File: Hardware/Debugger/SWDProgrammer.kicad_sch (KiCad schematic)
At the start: 37 parts, among them J1 USB_C_Receptacle_USB2.0, J2 USB_C_Receptacle_USB2.0, U1 AP2112K-3.3, U2 STM32F103C8Tx, Y1 32.768KHZ, Y2 8Mhz

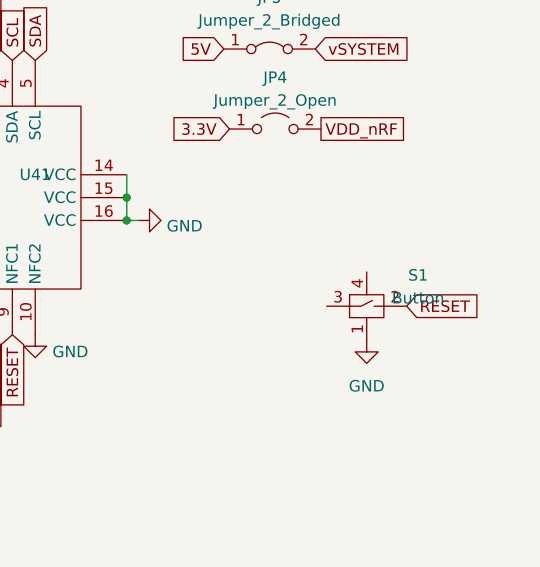
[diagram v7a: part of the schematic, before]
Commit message: migrated components to 0201
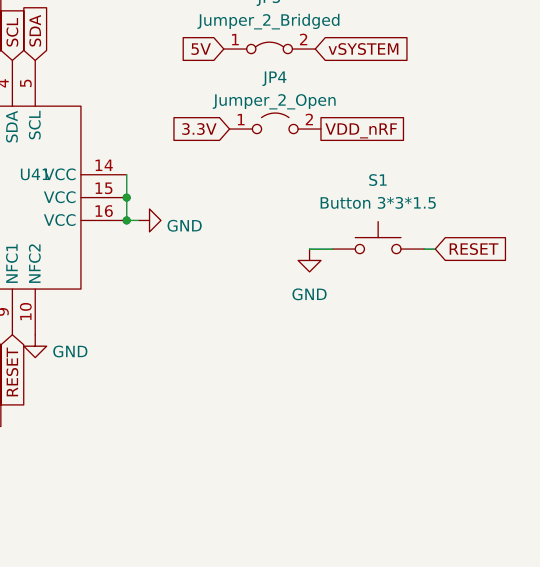
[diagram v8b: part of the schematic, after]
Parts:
- removed S1: Button, Library:button 3x3, symbol Library:Button
- added S1: Button 3*3*1.5, Library:button 3x3, symbol Switch:SW_Push
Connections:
- net GND: now also S1.1
- net RESET: now also S1.2
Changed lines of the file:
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@@
 	(wire
 		(pts
+			(xy 247.65 130.81) (xy 250.19 130.81)
+		)
+		(stroke
+			(width 0)
+			(type default)
+		)
+	)
+	(wire
+		(pts
 			(xy 131.445 20.955) (xy 140.335 20.955)
 		)
@@
 	(wire
 		(pts
+			(xy 261.62 130.81) (xy 260.35 130.81)
+		)
+		(stroke
+			(width 0)
+			(type default)
+		)
+	)
+	(wire
+		(pts
 			(xy 114.935 72.39) (xy 108.585 72.39)
 		)
@@
 		)
 	)
-	(global_label "RESET"
-		(shape input)
-		(at 258.445 137.16 0)
-		(fields_autoplaced yes)
-		(effects
-			(font
-				(size 1.27 1.27)
-			)
-			(justify left)
-		)
-		(property "Intersheetrefs" "${INTERSHEET_REFS}"
-			(at 267.0959 137.16 0)
-			(effects
-				(font
-					(size 1.27 1.27)
-				)
-				(justify left)
-				(hide yes)
-			)
-		)
-	)
 	(global_label "3.3V"
 		(shape input)
@@
 		)
 	)
+	(global_label "RESET"
+		(shape input)
+		(at 261.62 130.81 0)
+		(fields_autoplaced yes)
+		(effects
+			(font
+				(size 1.27 1.27)
+			)
+			(justify left)
+		)
+		(property "Intersheetrefs" "${INTERSHEET_REFS}"
+			(at 270.2709 130.81 0)
+			(effects
+				(font
+					(size 1.27 1.27)
+				)
+				(justify left)
+				(hide yes)
+			)
+		)
+	)
 	(global_label "3.3V"
 		(shape input)
@@
 	)
 	(symbol
-		(lib_id "power:GND")
-		(at 254 140.97 0)
-		(unit 1)
-		(exclude_from_sim no)
-		(in_bom yes)
-		(on_board yes)
-		(dnp no)
-		(fields_autoplaced yes)
-		(property "Reference" "#PWR026"
-			(at 254 147.32 0)
-			(effects
-				(font
-					(size 1.27 1.27)
-				)
-				(hide yes)
-			)
-		)
-		(property "Value" "GND"
-			(at 254 146.05 0)
-			(effects
-				(font
-					(size 1.27 1.27)
-				)
-			)
-		)
-		(property "Footprint" ""
-			(at 254 140.97 0)
-			(effects
-				(font
-					(size 1.27 1.27)
-				)
-				(hide yes)
-			)
-		)
-		(property "Datasheet" ""
-			(at 254 140.97 0)
-			(effects
-				(font
-					(size 1.27 1.27)
-				)
-				(hide yes)
-			)
-		)
-		(property "Description" ""
-			(at 254 140.97 0)
-			(effects
-				(font
-					(size 1.27 1.27)
-				)
-				(hide yes)
-			)
-		)
-		(pin "1"
-		)
-		(instances
-			(project "SWDProgrammer"
-				(path "/c10d4a68-1c04-4145-8c29-cc9b9e805c41"
-					(reference "#PWR026")
-					(unit 1)
-				)
-			)
-			(project "Revolute"
-				(path "/e63e39d7-6ac0-4ffd-8aa3-1841a4541b55"
-					(reference "#PWR034")
-					(unit 1)
-				)
-			)
-			(project "TopPCB"
-				(path "/ea7d4d47-b765-4ea1-81d3-52cfadd68d8d"
-					(reference "#PWR01")
-					(unit 1)
-				)
-			)
-		)
-	)
-	(symbol
 		(lib_id "Device:C")
 		(at 26.67 74.93 270)
@@
 	)
 	(symbol
+		(lib_id "Switch:SW_Push")
+		(at 255.27 130.81 0)
+		(unit 1)
+		(exclude_from_sim no)
+		(in_bom yes)
+		(on_board yes)
+		(dnp no)
+		(fields_autoplaced yes)
+		(property "Reference" "S1"
+			(at 255.27 123.19 0)
+			(effects
+				(font
+					(size 1.27 1.27)
+				)
+			)
+		)
+		(property "Value" "Button 3*3*1.5"
+			(at 255.27 125.73 0)
+			(effects
+				(font
+					(size 1.27 1.27)
+				)
+			)
+		)
+		(property "Footprint" "Library:button 3x3"
+			(at 255.27 125.73 0)
+			(effects
+				(font
+					(size 1.27 1.27)
+				)
+				(hide yes)
+			)
+		)
+		(property "Datasheet" "~"
+			(at 255.27 125.73 0)
+			(effects
+				(font
+					(size 1.27 1.27)
+				)
+				(hide yes)
+			)
+		)
+		(property "Description" "Push button switch, generic, two pins"
+			(at 255.27 130.81 0)
+			(effects
+				(font
+					(size 1.27 1.27)
+				)
+				(hide yes)
+			)
+		)
+		(property "ID" "111"
+			(at 255.27 130.81 0)
+			(effects
+				(font
+					(size 1.27 1.27)
+				)
+				(hide yes)
+			)
+		)
+		(pin "2"
+		)
+		(pin "1"
+		)
+		(instances
+			(project "SWDProgrammer"
+				(path "/c10d4a68-1c04-4145-8c29-cc9b9e805c41"
+					(reference "S1")
+					(unit 1)
+				)
+			)
+		)
+	)
+	(symbol
 		(lib_id "power:GND")
 		(at 180.975 53.975 0)
@@
 	(symbol
 		(lib_id "power:GND")
+		(at 247.65 130.81 0)
+		(unit 1)
+		(exclude_from_sim no)
+		(in_bom yes)
+		(on_board yes)
+		(dnp no)
+		(fields_autoplaced yes)
+		(property "Reference" "#PWR027"
+			(at 247.65 137.16 0)
+			(effects
+				(font
+					(size 1.27 1.27)
+				)
+				(hide yes)
+			)
+		)
+		(property "Value" "GND"
+			(at 247.65 135.89 0)
+			(effects
+				(font
+					(size 1.27 1.27)
+				)
+			)
+		)
+		(property "Footprint" ""
+			(at 247.65 130.81 0)
+			(effects
+				(font
+					(size 1.27 1.27)
+				)
+				(hide yes)
+			)
+		)
+		(property "Datasheet" ""
+			(at 247.65 130.81 0)
+			(effects
+				(font
+					(size 1.27 1.27)
+				)
+				(hide yes)
+			)
+		)
+		(property "Description" ""
+			(at 247.65 130.81 0)
+			(effects
+				(font
+					(size 1.27 1.27)
+				)
+				(hide yes)
+			)
+		)
+		(pin "1"
+		)
+		(instances
+			(project "SWDProgrammer"
+				(path "/c10d4a68-1c04-4145-8c29-cc9b9e805c41"
+					(reference "#PWR027")
+					(unit 1)
+				)
+			)
+		)
+	)
+	(symbol
+		(lib_id "power:GND")
 		(at 60.96 161.29 0)
 		(unit 1)
@@
 					(unit 1)
 				)
-			)
-		)
-	)
-	(symbol
-		(lib_id "Library:Button")
-		(at 252.095 135.255 0)
-		(unit 1)
-		(exclude_from_sim no)
-		(in_bom yes)
-		(on_board yes)
-		(dnp no)
-		(fields_autoplaced yes)
-		(property "Reference" "S1"
-			(at 259.715 133.7311 0)
-			(effects
-				(font
-					(size 1.27 1.27)
-				)
-			)
-		)
-		(property "Value" "Button"
-			(at 259.715 136.2711 0)
-			(effects
-				(font
-					(size 1.27 1.27)
-				)
-			)
-		)
-		(property "Footprint" "Library:button 3x3"
-			(at 254 141.605 0)
-			(effects
-				(font
-					(size 1.27 1.27)
-				)
-				(hide yes)
-			)
-		)
-		(property "Datasheet" ""
-			(at 252.095 135.255 0)
-			(effects
-				(font
-					(size 1.27 1.27)
-				)
-				(hide yes)
-			)
-		)
-		(property "Description" ""
-			(at 252.095 135.255 0)
-			(effects
-				(font
-					(size 1.27 1.27)
-				)
-				(hide yes)
-			)
-		)
-		(property "ID" "111"
-			(at 252.095 135.255 0)
-			(effects
-				(font
-					(size 1.27 1.27)
-				)
-				(hide yes)
-			)
-		)
-		(pin "1"
-		)
-		(pin "2"
-		)
-		(pin "3"
-		)
-		(pin "4"
-		)
-		(instances
-			(project "SWDProgrammer"
-				(path "/c10d4a68-1c04-4145-8c29-cc9b9e805c41"
-					(reference "S1")
-					(unit 1)
-				)
